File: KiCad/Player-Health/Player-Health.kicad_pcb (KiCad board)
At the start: 2 copper layers, 32 parts, among them IC1 ATMEGA328-P, J1 MICRO_USB, M1 RUMBLE, P1 2P_CGRID_M, P2 6pM CGrid, P3 6pM Header, P4 8pF Header, Q1 NPN, U1 MCP73831, U2 LM1084IT-3.3/NOPB, U3 14SLED, U4 ESP8266, X1 CRYSTAL

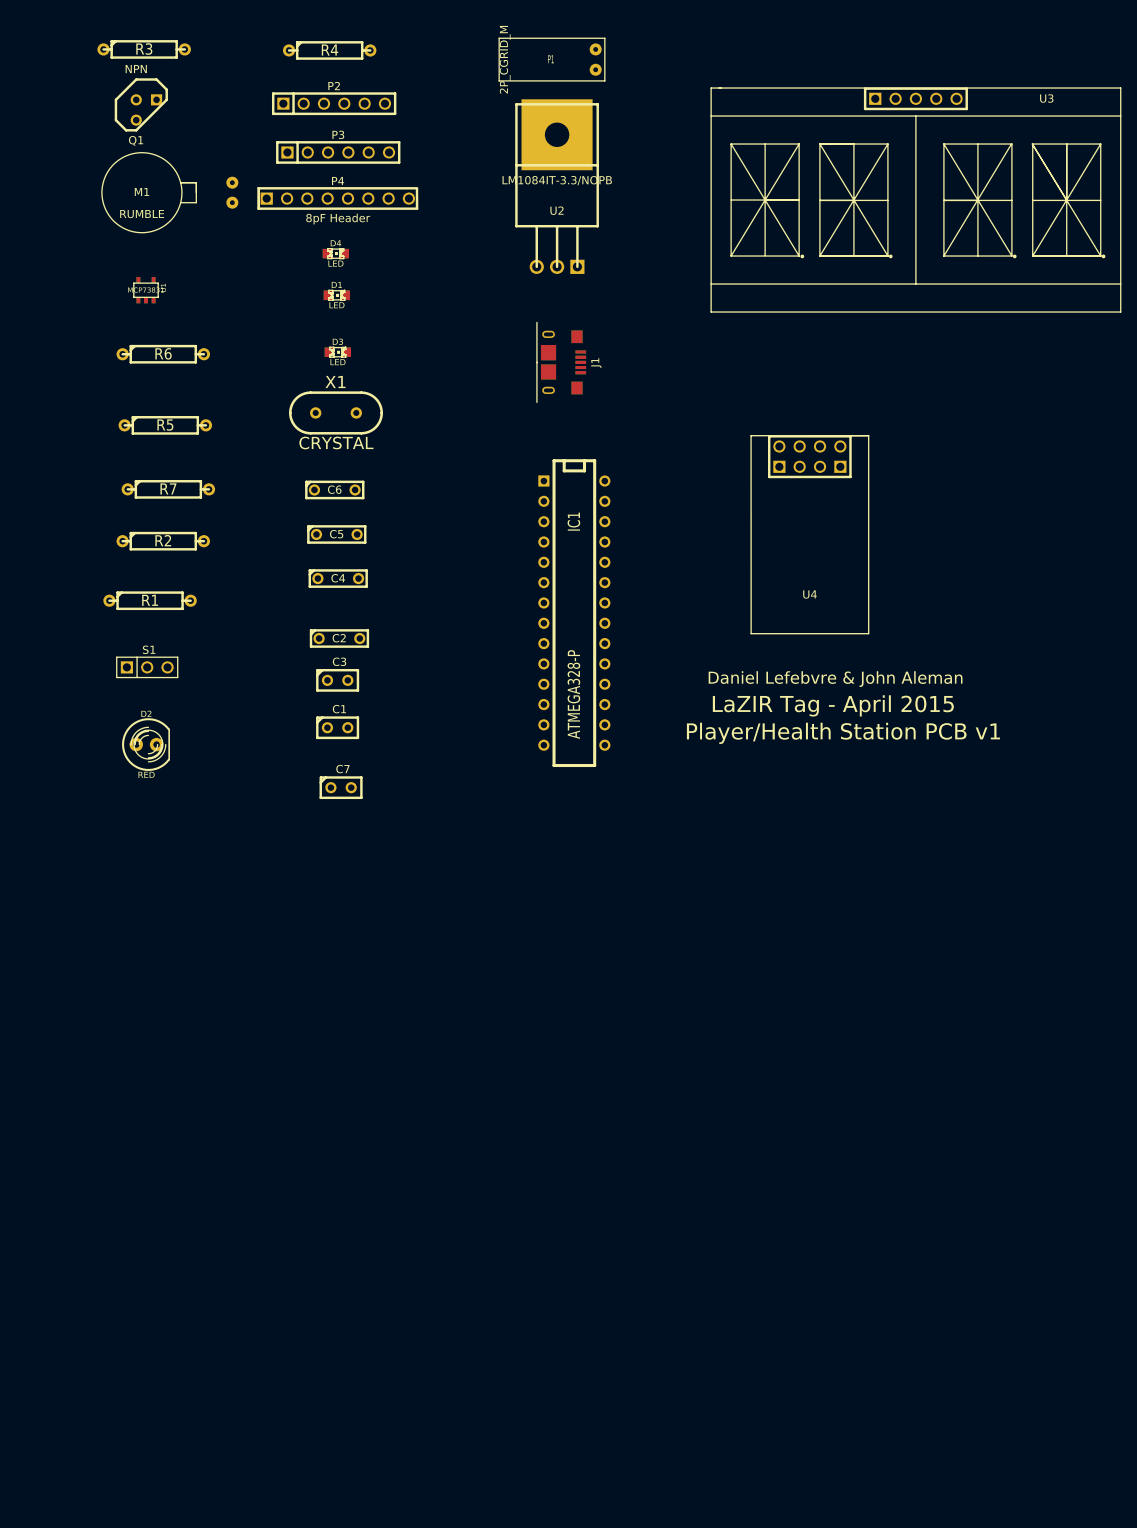
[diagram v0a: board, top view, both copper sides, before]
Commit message: Quick Update #2 4/17
Added Jumpers to Schematic, Net List and PCB, but failing connectivity
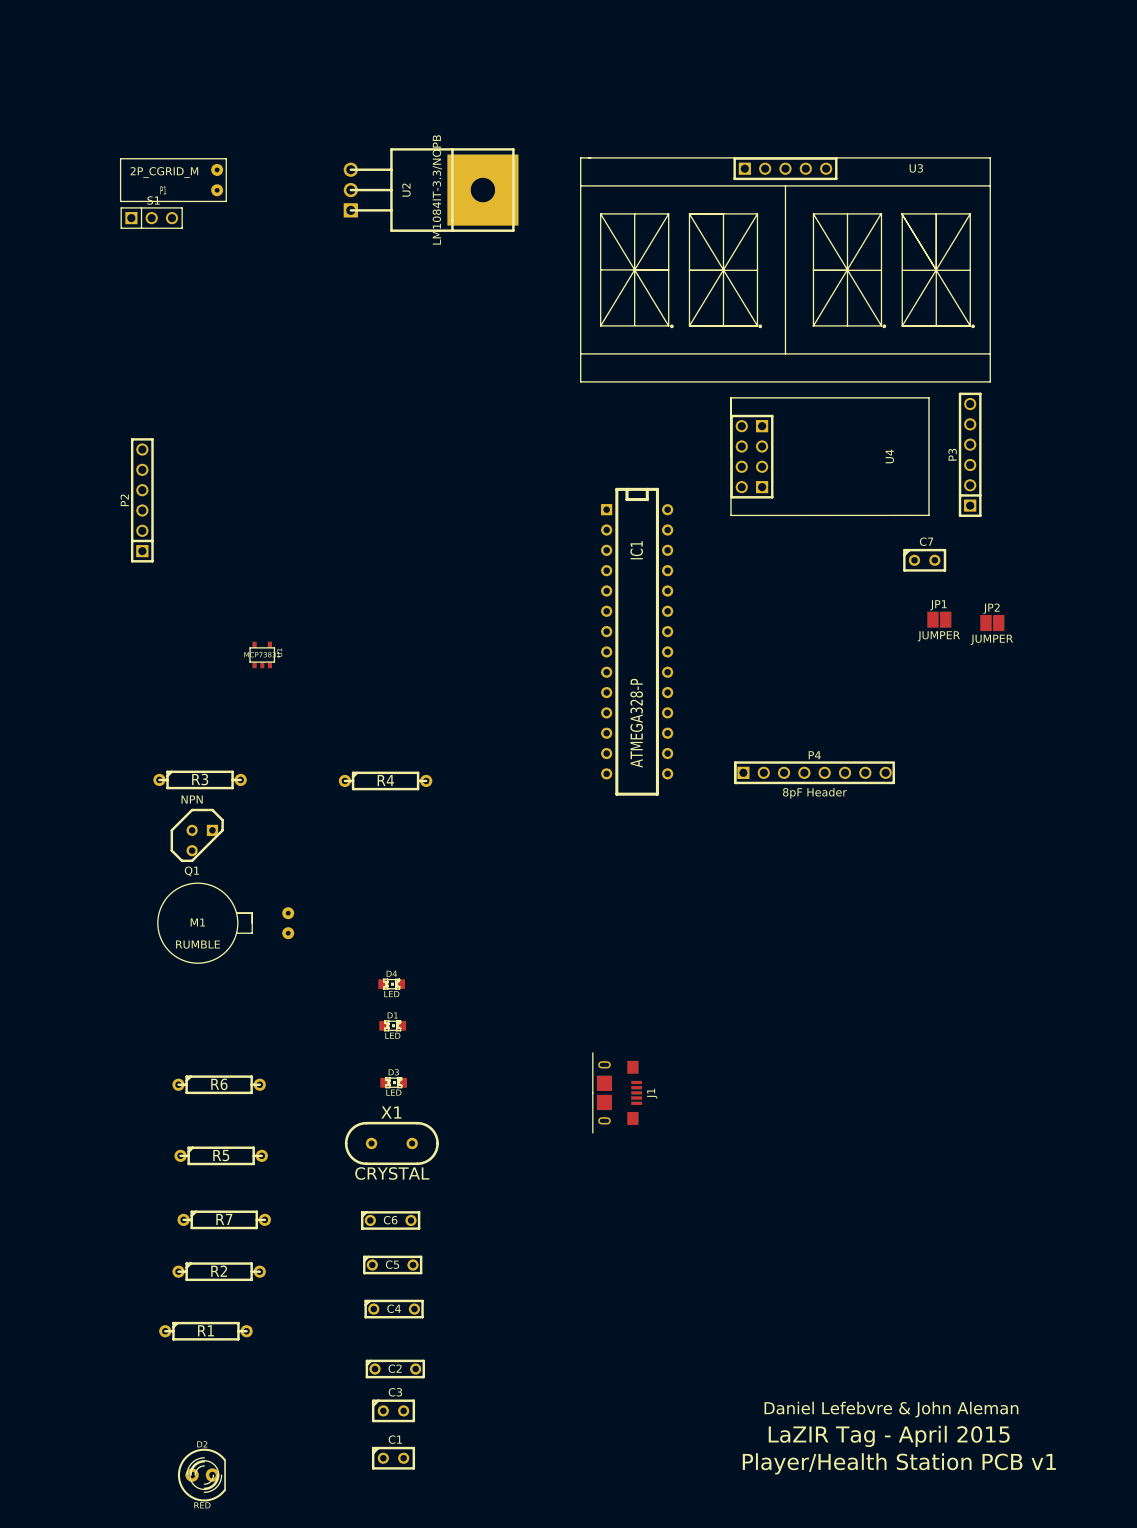
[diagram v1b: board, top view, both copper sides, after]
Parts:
- added JP1: JUMPER, JP, F.Cu at (125.4, 89.6)
- added JP2: JUMPER, JP, F.Cu at (132.0, 90.0)
- moved P4 93.3 mm to (109.8, 108.7)
- moved R6 91.6 mm to (35.4, 147.7)
- moved X1 91.6 mm to (57.0, 155.1)
- moved C2 91.6 mm to (57.4, 183.3)
- moved C3 91.6 mm to (57.2, 188.5)
- moved C4 91.6 mm to (57.3, 175.8)
- moved C5 91.6 mm to (57.1, 170.3)
- moved C6 91.6 mm to (56.8, 164.7)
- moved D2 91.6 mm to (33.3, 196.5)
- moved D4 91.6 mm to (56.9, 135.2)
- moved J1 91.6 mm to (83.5, 148.7)
- moved M1 91.6 mm to (32.7, 127.5)
- moved Q1 91.6 mm to (33.3, 117.2)
- moved R2 91.6 mm to (35.4, 171.1)
- moved R3 91.6 mm to (33.0, 109.6)
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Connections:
- U4 pad 6: (no net) -> N-0000022

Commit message: Quick Update #3 4/17
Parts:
- moved JP2 31.8 mm to (101.7, 80.5)
- moved JP1 23.6 mm to (102.0, 86.4)
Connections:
- IC1 pad 3: UART TX -> N-0000025
- U4 pad 6: N-0000022 (its old number) -> (no net)
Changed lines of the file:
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@@
 (kicad_pcb (version 3) (host pcbnew "(2013-07-07 BZR 4022)-stable")
   (general
-    (links 73)
-    (no_connects 73)
+    (links 72)
+    (no_connects 72)
     (area 20.410312 25.939045 143.355526 203.48)
     (thickness 1.6)
@@
     (mod_text_size 1 1)
     (mod_text_width 0.15)
-    (pad_size 1.4 2)
-    (pad_drill 0)
+    (pad_size 1.524 1.524)
+    (pad_drill 1.016)
     (pad_to_mask_clearance 0)
     (aux_axis_origin 0 0)
@@
   (net 9 MISO)
   (net 10 MOSI)
-  (net 11 N-000001)
-  (net 12 N-0000015)
-  (net 13 N-0000017)
-  (net 14 N-0000019)
-  (net 15 N-000002)
-  (net 16 N-0000022)
-  (net 17 N-0000023)
-  (net 18 N-0000026)
-  (net 19 N-0000029)
-  (net 20 N-0000030)
-  (net 21 N-000004)
-  (net 22 N-000005)
-  (net 23 N-000006)
+  (net 11 N-0000017)
+  (net 12 N-0000020)
+  (net 13 N-0000022)
+  (net 14 N-0000025)
+  (net 15 N-0000026)
+  (net 16 N-0000029)
+  (net 17 N-000003)
+  (net 18 N-0000030)
+  (net 19 N-0000031)
+  (net 20 N-000004)
+  (net 21 N-000005)
+  (net 22 N-000006)
+  (net 23 N-000007)
   (net 24 Reset)
   (net 25 Rumble)
@@
     (add_net MISO)
     (add_net MOSI)
-    (add_net N-000001)
-    (add_net N-0000015)
     (add_net N-0000017)
-    (add_net N-0000019)
-    (add_net N-000002)
+    (add_net N-0000020)
     (add_net N-0000022)
-    (add_net N-0000023)
+    (add_net N-0000025)
     (add_net N-0000026)
     (add_net N-0000029)
+    (add_net N-000003)
     (add_net N-0000030)
+    (add_net N-0000031)
     (add_net N-000004)
     (add_net N-000005)
     (add_net N-000006)
+    (add_net N-000007)
     (add_net Reset)
     (add_net Rumble)
@@
     (pad 1 thru_hole rect (at 1.27 -1.27) (size 1.397 1.397) (drill 0.8128)
       (layers *.Cu *.Mask F.SilkS)
-      (net 17 N-0000023)
+      (net 12 N-0000020)
     )
     (pad 2 thru_hole circle (at -1.27 -1.27) (size 1.397 1.397) (drill 0.8128)
       (layers *.Cu *.Mask F.SilkS)
-      (net 13 N-0000017)
+      (net 11 N-0000017)
     )
     (pad 3 thru_hole circle (at -1.27 1.27) (size 1.397 1.397) (drill 0.8128)
@@
     (pad 2 thru_hole circle (at 0 -2.54) (size 1.778 1.778) (drill 1.143)
       (layers *.Cu *.Mask F.SilkS)
-      (net 21 N-000004)
+      (net 16 N-0000029)
     )
     (pad 3 thru_hole circle (at 0 0) (size 1.778 1.778) (drill 1.143)
       (layers *.Cu *.Mask F.SilkS)
-      (net 22 N-000005)
+      (net 20 N-000004)
     )
     (pad 4 thru_hole rect (at 16.51 0) (size 8.89 8.89) (drill 3.048)
@@
     (pad 1 smd rect (at -0.9525 1.27) (size 0.508 0.762)
       (layers F.Cu F.Paste F.Mask)
-      (net 20 N-0000030)
+      (net 19 N-0000031)
     )
     (pad 3 smd rect (at 0.9525 1.27) (size 0.508 0.762)
@@
     (pad 5 smd rect (at -0.9525 -1.27) (size 0.508 0.762)
       (layers F.Cu F.Paste F.Mask)
-      (net 11 N-000001)
+      (net 22 N-000006)
     )
     (pad 2 smd rect (at 0 1.27) (size 0.508 0.762)
@@
     (pad 1 thru_hole circle (at 11.3 1.25) (size 1.5 1.5) (drill 0.6)
       (layers *.Cu *.Mask F.SilkS)
-      (net 17 N-0000023)
+      (net 12 N-0000020)
     )
   )
@@
     (pad 2 thru_hole circle (at 5.08 0) (size 1.524 1.524) (drill 0.8128)
       (layers *.Cu *.Mask F.SilkS)
-      (net 12 N-0000015)
+      (net 17 N-000003)
     )
     (model discret/resistor.wrl
@@
     (pad 2 thru_hole circle (at 5.08 0) (size 1.524 1.524) (drill 0.8128)
       (layers *.Cu *.Mask F.SilkS)
-      (net 13 N-0000017)
+      (net 11 N-0000017)
     )
     (model discret/resistor.wrl
@@
     (pad 1 thru_hole circle (at -5.08 0) (size 1.524 1.524) (drill 0.8128)
       (layers *.Cu *.Mask F.SilkS)
-      (net 22 N-000005)
+      (net 20 N-000004)
     )
     (pad 2 thru_hole circle (at 5.08 0) (size 1.524 1.524) (drill 0.8128)
@@
     (pad 2 thru_hole circle (at 5.08 0) (size 1.524 1.524) (drill 0.8128)
       (layers *.Cu *.Mask F.SilkS)
-      (net 15 N-000002)
+      (net 23 N-000007)
     )
     (model discret/resistor.wrl
@@
     (pad 1 thru_hole circle (at -5.08 0) (size 1.524 1.524) (drill 0.8128)
       (layers *.Cu *.Mask F.SilkS)
-      (net 11 N-000001)
+      (net 22 N-000006)
     )
     (pad 2 thru_hole circle (at 5.08 0) (size 1.524 1.524) (drill 0.8128)
@@
     (pad 1 thru_hole rect (at -2.54 0) (size 1.524 1.524) (drill 1.016)
       (layers *.Cu *.Mask F.SilkS)
-      (net 23 N-000006)
+      (net 21 N-000005)
     )
     (pad 2 thru_hole circle (at 0 0) (size 1.524 1.524) (drill 1.016)
@@
     (pad 1 thru_hole circle (at -1.27 0) (size 1.6764 1.6764) (drill 0.8128)
       (layers *.Cu *.Mask F.SilkS)
-      (net 15 N-000002)
+      (net 23 N-000007)
     )
     (pad 2 thru_hole circle (at 1.27 0) (size 1.6764 1.6764) (drill 0.8128)
       (layers *.Cu *.Mask F.SilkS)
-      (net 20 N-0000030)
+      (net 19 N-0000031)
     )
     (model discret/leds/led5_vertical_verde.wrl
@@
     (pad 1 smd rect (at -1.04902 0) (size 1.19888 1.19888)
       (layers F.Cu F.Paste F.Mask)
-      (net 12 N-0000015)
+      (net 17 N-000003)
     )
     (pad 2 smd rect (at 1.04902 0) (size 1.19888 1.19888)
@@
     (pad 2 smd rect (at 1.04902 0) (size 1.19888 1.19888)
       (layers F.Cu F.Paste F.Mask)
-      (net 22 N-000005)
+      (net 20 N-000004)
     )
   )
@@
     (pad 1 smd rect (at -1.04902 0) (size 1.19888 1.19888)
       (layers F.Cu F.Paste F.Mask)
-      (net 21 N-000004)
+      (net 16 N-0000029)
     )
     (pad 2 smd rect (at 1.04902 0) (size 1.19888 1.19888)
@@
     (pad 1 thru_hole circle (at -2.54 0) (size 1.4224 1.4224) (drill 0.762)
       (layers *.Cu *.Mask F.SilkS)
-      (net 18 N-0000026)
+      (net 15 N-0000026)
     )
     (pad 2 thru_hole circle (at 2.54 0) (size 1.4224 1.4224) (drill 0.762)
       (layers *.Cu *.Mask F.SilkS)
-      (net 19 N-0000029)
+      (net 18 N-0000030)
     )
     (model discret/xtal/crystal_hc18u_vertical.wrl
@@
     (pad 3 thru_hole circle (at -11.43 3.81 270) (size 1.397 1.397) (drill 0.8128)
       (layers *.Cu *.Mask F.SilkS)
-      (net 28 "UART TX")
+      (net 14 N-0000025)
     )
     (pad 4 thru_hole circle (at -8.89 3.81 270) (size 1.397 1.397) (drill 0.8128)
@@
     (pad 9 thru_hole circle (at 3.81 3.81 270) (size 1.397 1.397) (drill 0.8128)
       (layers *.Cu *.Mask F.SilkS)
-      (net 19 N-0000029)
+      (net 18 N-0000030)
     )
     (pad 10 thru_hole circle (at 6.35 3.81 270) (size 1.397 1.397) (drill 0.8128)
       (layers *.Cu *.Mask F.SilkS)
-      (net 18 N-0000026)
+      (net 15 N-0000026)
     )
     (pad 11 thru_hole circle (at 8.89 3.81 270) (size 1.397 1.397) (drill 0.8128)
@@
     (pad 1 thru_hole circle (at -2.54 0) (size 1.397 1.397) (drill 0.8128)
       (layers *.Cu *.Mask F.SilkS)
-      (net 19 N-0000029)
+      (net 18 N-0000030)
     )
     (pad 2 thru_hole circle (at 2.54 0) (size 1.397 1.397) (drill 0.8128)
@@
     (pad 1 thru_hole circle (at -2.54 0) (size 1.397 1.397) (drill 0.8128)
       (layers *.Cu *.Mask F.SilkS)
-      (net 18 N-0000026)
+      (net 15 N-0000026)
     )
     (pad 2 thru_hole circle (at 2.54 0) (size 1.397 1.397) (drill 0.8128)
@@
     (pad 1 thru_hole circle (at -1.27 0) (size 1.397 1.397) (drill 0.8128)
       (layers *.Cu *.Mask F.SilkS)
-      (net 21 N-000004)
+      (net 16 N-0000029)
     )
     (pad 2 thru_hole circle (at 1.27 0) (size 1.397 1.397) (drill 0.8128)
@@
     (pad 1 thru_hole circle (at -1.27 0) (size 1.397 1.397) (drill 0.8128)
       (layers *.Cu *.Mask F.SilkS)
-      (net 14 N-0000019)
+      (net 13 N-0000022)
     )
     (pad 2 thru_hole circle (at 1.27 0) (size 1.397 1.397) (drill 0.8128)
@@
     (pad 2 thru_hole circle (at -1.27 0 270) (size 1.5 1.5) (drill 0.6)
       (layers *.Cu *.Mask F.SilkS)
-      (net 23 N-000006)
+      (net 21 N-000005)
     )
   )
@@
     (pad 6 thru_hole circle (at 6.35 0 90) (size 1.524 1.524) (drill 1.016)
       (layers *.Cu *.Mask F.SilkS)
-      (net 14 N-0000019)
+      (net 13 N-0000022)
     )
     (model pin_array/pins_array_6x1.wrl
@@
     (pad 6 thru_hole circle (at 1.27 -1.27 90) (size 1.524 1.524) (drill 1.016)
       (layers *.Cu *.Mask F.SilkS)
-      (net 16 N-0000022)
     )
     (pad 7 thru_hole rect (at 3.81 1.27 90) (size 1.524 1.524) (drill 1.016)
@@
   )
   (module JP (layer F.Cu)
-    (at 132.0292 90.0176)
+    (at 101.6762 80.4672)
     (fp_text reference JP2 (at 0 -1.89) (layer F.SilkS)
       (effects (font (size 1 1) (thickness 0.15)))
@@
   )
   (module JP (layer F.Cu)
-    (at 125.3998 89.5858)
+    (at 101.981 86.4108)
     (fp_text reference JP1 (at 0 -1.89) (layer F.SilkS)
       (effects (font (size 1 1) (thickness 0.15)))

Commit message: Last Update for the Night 4/17(4/16)
General PCB layout, fix to jumper pads
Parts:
- JP1, JP2: footprint JP -> JumperPads
- moved D2 177.5 mm to (57.7, 20.7)
- moved C2 162.9 mm to (43.6, 20.9)
- moved C3 152.4 mm to (42.7, 36.8), turned to 270 degrees
- moved C4 151.8 mm to (43.8, 24.5)
- moved R1 151.2 mm to (43.3, 27.7)
- moved J1 138.1 mm to (23.5, 24.4)
- moved R7 137.8 mm to (89.3, 37.6), turned to 90 degrees
- moved C1 131.0 mm to (72.8, 64.3), turned to 270 degrees
- moved R2 128.7 mm to (45.0, 42.8)
- moved D3 117.8 mm to (48.6, 30.0)
- moved D1 103.3 mm to (34.7, 39.5)
- moved C6 100.3 mm to (64.3, 64.7), turned to 270 degrees
- moved C5 98.3 mm to (64.3, 72.3), turned to 90 degrees
- moved R4 93.8 mm to (44.2, 16.8)
- moved X1 87.1 mm to (68.5, 68.8), turned to 90 degrees
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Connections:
- JP1 pad 1: (no net) -> N-0000025
- JP1 pad 2: (no net) -> UART TX
- JP2 pad 1: (no net) -> N-000001
- JP2 pad 2: (no net) -> GND
- U4 pad 6: (no net) -> N-000001
